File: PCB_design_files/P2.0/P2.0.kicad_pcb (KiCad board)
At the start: 4 copper layers, 18.5 x 18 mm, 58 parts, among them J1 EEG_IN, J2 20021121-00008C4LF, U1 INA819IDRGR, U2 TLV9102, U3 TPS61094, U4 TPS60400, U5 NRF52832-QFAA-R, Y1 32MHz

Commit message: Updated schematic
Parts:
- BT1, J1: moved to F.Cu
- C19, C20: footprint Capacitor_SMD:C_0402_1005Metric -> Capacitor_SMD:C_0603_1608Metric
- R20: moved to B.Cu
- moved C8 56.7 mm to (32.3, 77.2)
- moved L1 52.6 mm to (29.3, 67.6), turned to 180 degrees
- moved R19 52.0 mm to (32.5, 72.9), turned to 180 degrees
- moved U3 46.6 mm to (41.4, 71.5)
- moved C9 45.7 mm to (44.4, 69.7), turned to 90 degrees
- moved C10 44.7 mm to (46.6, 70.8)
- moved C11 41.7 mm to (46.4, 73.2)
- moved R17 39.9 mm to (113.0, 48.9), turned to 180 degrees
- moved U4 39.8 mm to (50.5, 71.1), turned to -90 degrees
- moved J2 39.7 mm to (77.7, 83.7)
- moved R16 38.2 mm to (113.0, 47.9), turned to 0 degrees
- moved C7 33.4 mm to (113.0, 46.9)
- moved R14 31.5 mm to (113.0, 45.9), turned to 0 degrees
- moved R12 30.0 mm to (92.0, 24.3), turned to 180 degrees
- moved R13 27.4 mm to (92.0, 26.3)
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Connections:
- U1 pad 9: (no net) -> -3V3
- U3 pad 13: (no net) -> GND
- U5 pad 49: unconnected-(U5-EPAD-Pad49) -> GND
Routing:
- net GND: track 39.9 -> 20.6 mm, vias 31 -> 13
- net Net-(BT1-+): track 16.2 -> 0.00 mm
- net +3V3: track 21.0 -> 4.83 mm, vias 7 -> 2
- net STAGE_3_OUT: track 7.70 -> 0.00 mm, vias 1 -> 0
- net /EEG+: track 6.87 -> 0.00 mm
- net /EEG-: track 6.62 -> 0.00 mm
- net Net-(U4-CFLY-): track 4.37 -> 0.00 mm
- net -3V3: track 5.62 -> 1.71 mm, vias 1 -> 0
- net Net-(U2-IN1+): track 3.07 -> 0.00 mm
- net Net-(U5-P0.02/AIN0): track 2.35 -> 0.00 mm
- net Net-(R3-Pad2): track 1.94 -> 0.00 mm
- net Net-(R3-Pad1): track 1.94 -> 0.00 mm
- net Net-(U4-CFLY+): track 1.71 -> 0.00 mm
- net Net-(C7-Pad1): track 1.50 -> 0.00 mm
- net Net-(U1-OUT): track 1.44 -> 0.00 mm
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- removed copper zone on B.Cu, net +3V3
- removed copper zone on B.Cu, net GND
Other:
- board size 18.5 x 18 mm -> 19 x 19 mm

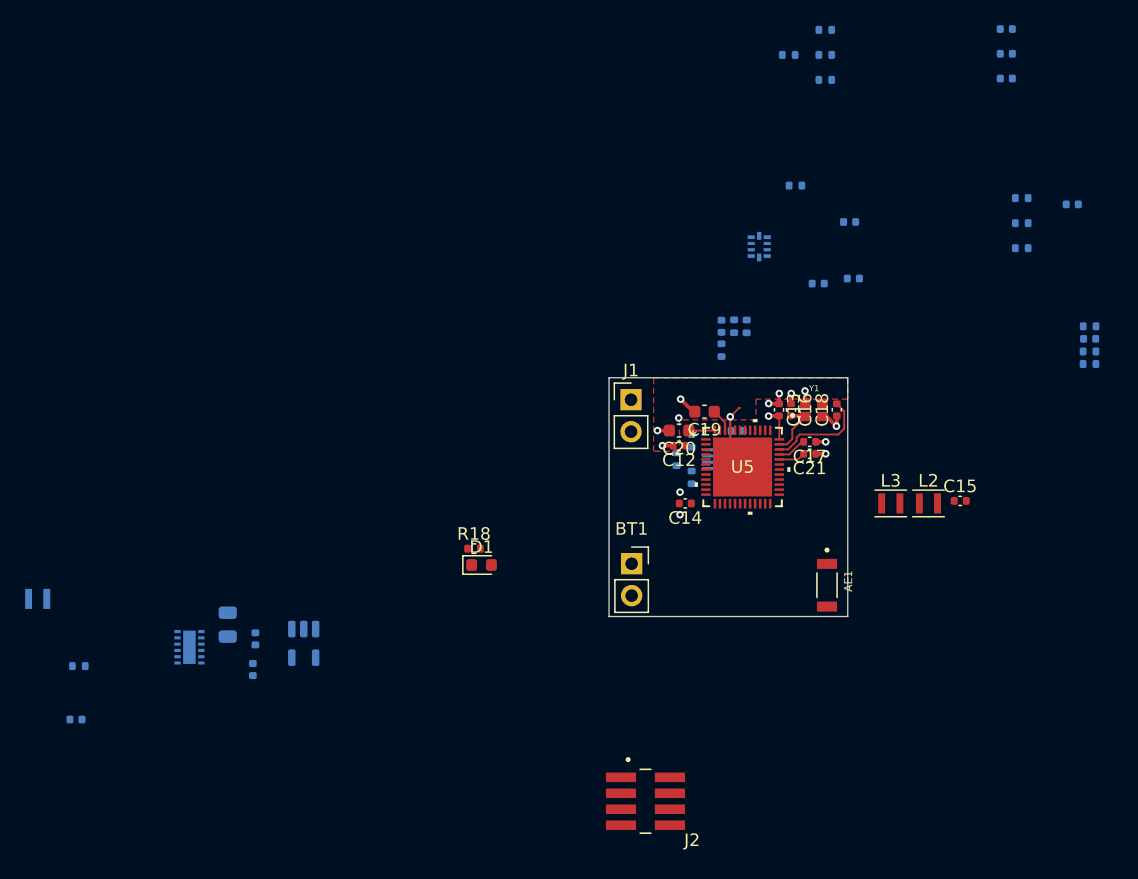
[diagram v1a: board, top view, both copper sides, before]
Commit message: made some schematic updates
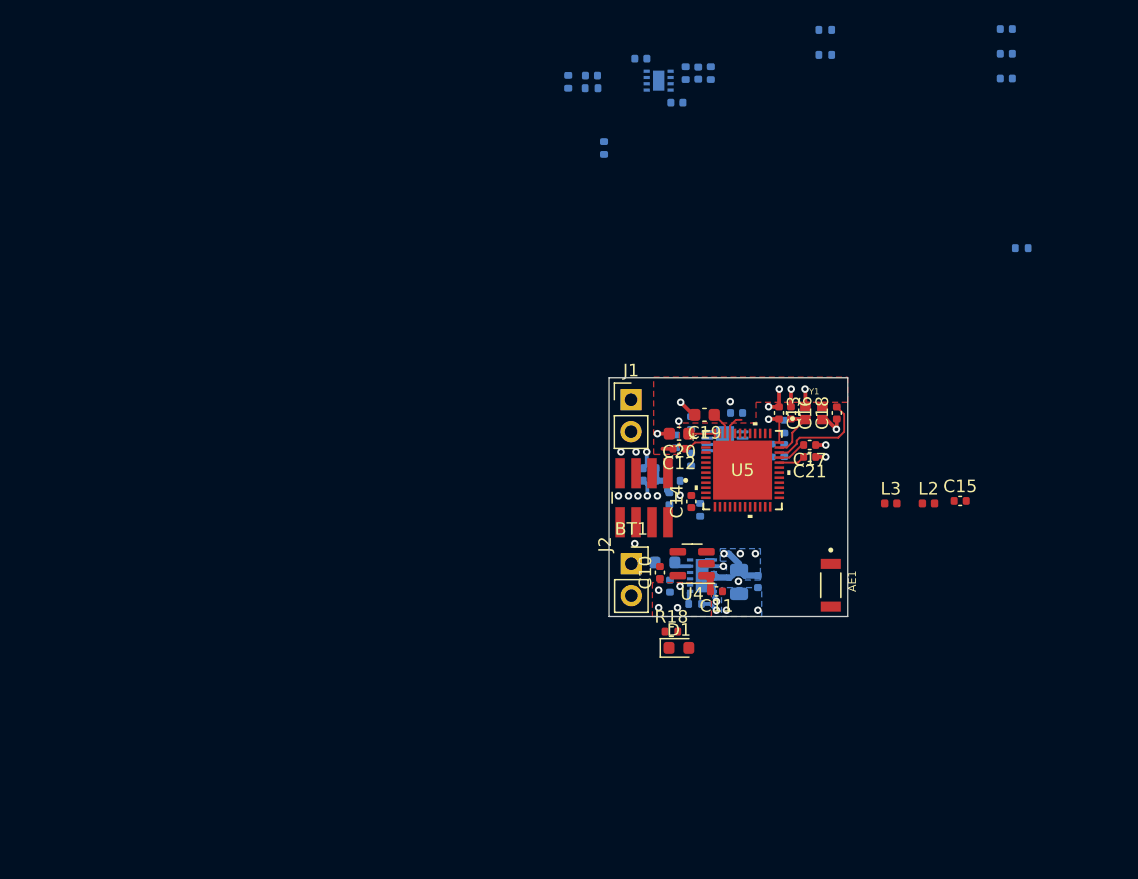
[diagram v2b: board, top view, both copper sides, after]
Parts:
- added C26: 0.1uF, Capacitor_SMD:C_0402_1005Metric, B.Cu at (86.6, 66.2)
- C10, C11, U4: moved to F.Cu
- C12, C13, C14: value 100nF -> 0.1uF
- C22, C23: value .1uF -> 0.1uF
- C24, C25: value .1uF -> 1uF
- L1: footprint Inductor_SMD:L_Murata_DFE201610P -> Inductor_SMD:L_0603_1608Metric
- L2, L3: footprint Inductor_SMD:L_Murata_DFE201610P -> Inductor_SMD:L_0402_1005Metric
- R19: value 1.1k -> 4.75k
- U2: value TLV9102 -> TLV9102IDSGR; footprint Package_DFN_QFN:Texas_R-PUQFN-N10 -> Package_SON:WSON-8-1EP_2x2mm_P0.5mm_EP0.9x1.6mm
- moved L1 50.0 mm to (79.2, 64.7), turned to 0 degrees
- moved R19 49.3 mm to (81.6, 68.0), turned to 0 degrees
- moved C8 48.5 mm to (79.6, 66.6), turned to 90 degrees
- moved U3 41.2 mm to (82.2, 65.8)
- moved C9 40.8 mm to (85.1, 66.2)
- moved C11 37.4 mm to (83.3, 67.0), turned to 180 degrees
- moved R16 36.5 mm to (78.0, 58.2), turned to 180 degrees
- moved R17 36.0 mm to (78.0, 57.2), turned to 0 degrees
- moved C7 35.8 mm to (79.5, 59.6), turned to 90 degrees
- moved R8 35.3 mm to (73.4, 26.9), turned to 0 degrees
- moved R20 35.1 mm to (79.9, 58.2), turned to 0 degrees
- moved R14 34.3 mm to (82.0, 60.5), turned to 90 degrees
- moved R9 33.8 mm to (74.3, 31.7), turned to -90 degrees
- moved C10 32.6 mm to (78.8, 65.5)
- moved U4 31.6 mm to (81.4, 64.8), turned to 180 degrees
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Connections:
- C2 pad 1: Net-(U2-IN1+) -> Net-(U2-OUT1)
- C24 pad 1: +3V3 -> GND
- C24 pad 2: GND -> -3V3
- C25 pad 2: -3V3 -> +3V3
- J2 pad 4: GND -> -3V3
- J2 pad 5: SWO -> NRST
- J2 pad 6: NRST -> SWO
- J2 pad 7: SWDIO -> SWDCLK
- J2 pad 8: SWDCLK -> SWDIO
- R6 pad 1: Net-(U2-IN1+) -> Net-(U2-OUT1)
- U1 pad 9: -3V3 -> (no net)
- U2 pad 1: -3V3 -> Net-(U2-OUT1)
- U2 pad 2: unconnected-(U2-SHDN1-Pad2) -> Net-(U2-IN1-)
- U2 pad 3: unconnected-(U2-SHDN2-Pad3) -> Net-(U2-IN1+)
- U2 pad 4: Net-(U2-IN2+) -> -3V3
- U2 pad 5: Net-(U2-IN2-) -> Net-(U2-IN2+)
- U2 pad 6: Net-(U2-OUT2) -> Net-(U2-IN2-)
- U2 pad 7: +3V3 -> Net-(U2-OUT2)
- U2 pad 8: Net-(U2-IN1+) -> +3V3
- U2 pad 9: Net-(U2-IN1-) -> (no net)
- U3 pad 13: GND -> (no net)
- U5 pad 49: GND -> unconnected-(U5-EPAD-Pad49)
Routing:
- net +3V3: track 4.83 -> 16.8 mm, vias 2 -> 6
- net GND: track 20.6 -> 26.1 mm, vias 13 -> 21
- net STAGE_3_OUT: track 0.00 -> 2.90 mm
- net Net-(U5-DEC1): track 0.00 -> 1.86 mm
- net Net-(U3-SW): track 0.00 -> 1.34 mm
- net Net-(U3-OSEL): track 0.00 -> 1.05 mm
- net -3V3: track 1.71 -> 1.38 mm, vias 0 -> 4
- net SWO: vias 0 -> 1
- net SWDIO: vias 0 -> 1
- net SWDCLK: vias 0 -> 1
- net NRST: vias 0 -> 1
- added copper zone on B.Cu, net +3V3
- added copper zone on F.Cu, net -3V3
- added copper zone on B.Cu, net GND

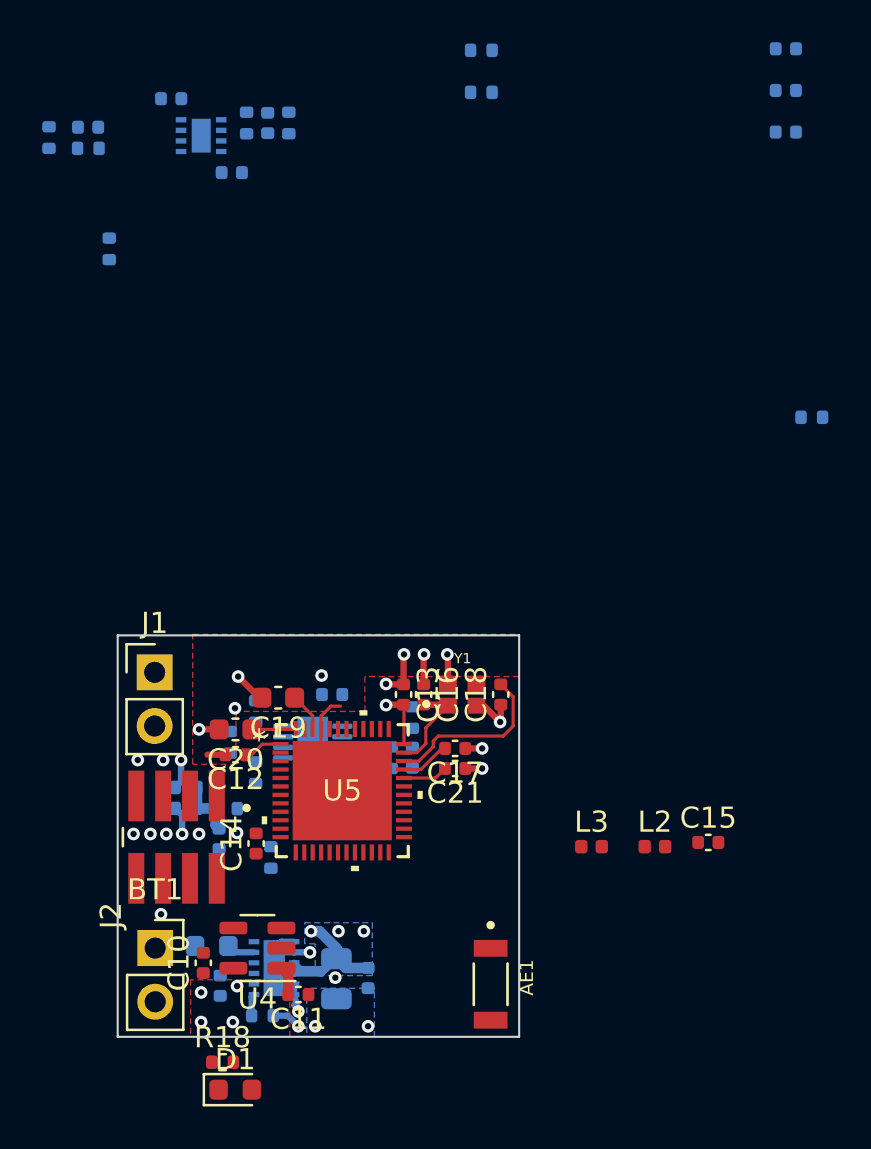
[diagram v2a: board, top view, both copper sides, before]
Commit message: Schematic updates
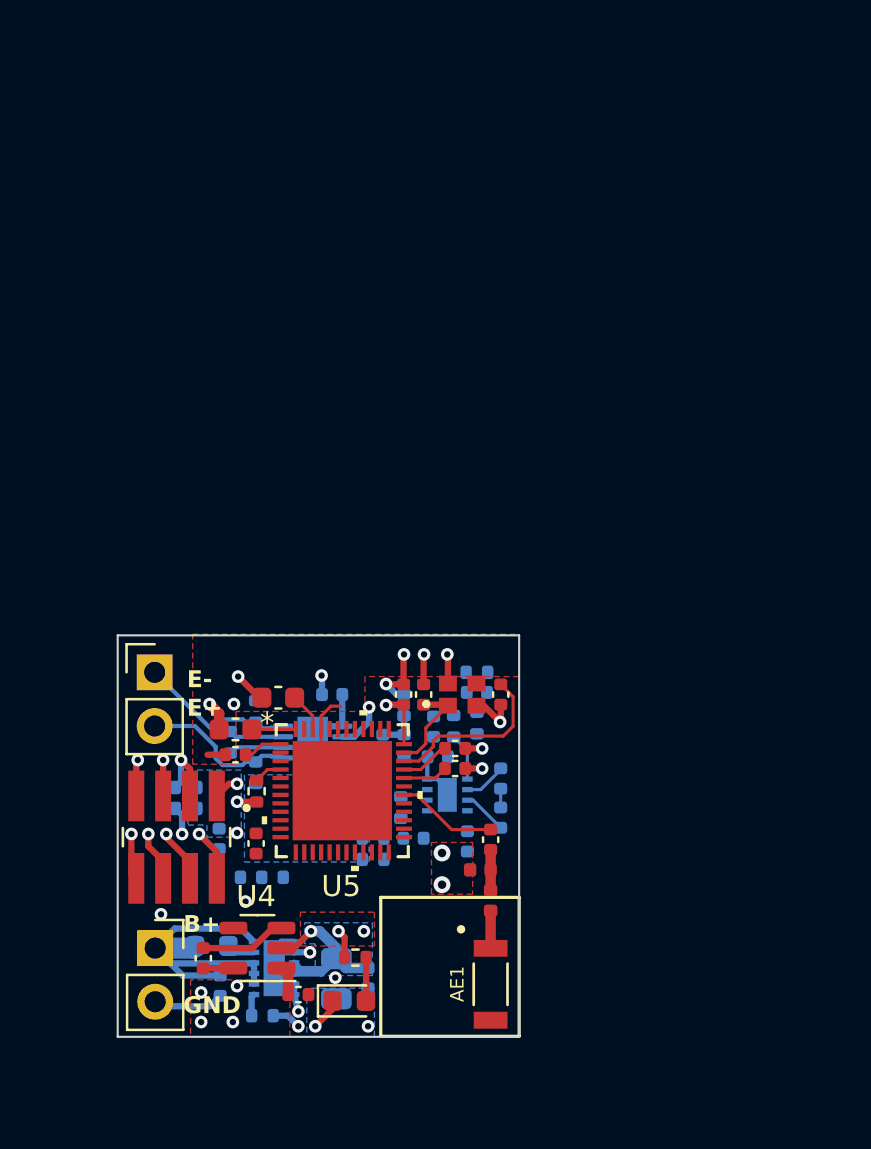
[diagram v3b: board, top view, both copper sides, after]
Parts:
- R20: moved to F.Cu
- moved C3 38.1 mm to (92.9, 58.6), turned to 90 degrees
- moved C25 37.8 mm to (91.3, 59.8), turned to 90 degrees
- moved R13 36.6 mm to (82.1, 61.5), turned to 0 degrees
- moved C4 36.2 mm to (89.7, 54.3), turned to -90 degrees
- moved C2 34.5 mm to (88.8, 59.6), turned to 180 degrees
- moved C6 33.4 mm to (92.9, 56.8), turned to -90 degrees
- moved U2 33.3 mm to (90.3, 57.5), turned to 0 degrees
- moved R6 33.2 mm to (88.2, 58.1), turned to 90 degrees
- moved R7 32.1 mm to (86.8, 57.6), turned to 180 degrees
- moved C5 32.0 mm to (91.8, 52.7), turned to 0 degrees
- moved R11 32.0 mm to (90.7, 54.3), turned to -90 degrees
- moved R8 30.9 mm to (91.8, 51.8), turned to 180 degrees
- moved R9 30.6 mm to (86.8, 59.6), turned to 180 degrees
- moved R12 29.9 mm to (91.8, 54.1), turned to -90 degrees
- moved R10 29.5 mm to (86.8, 60.6)
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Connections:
- R18 pad 1: Net-(BT1-+) -> +3V3
- U1 pad 9: (no net) -> -3V3
- U2 pad 9: (no net) -> -3V3
- U5 pad 49: unconnected-(U5-EPAD-Pad49) -> GND
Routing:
- net Net-(BT1-+): track 0.00 -> 16.8 mm
- net GND: track 26.1 -> 37.0 mm, vias 21 -> 25
- net /EEG-: track 0.00 -> 8.10 mm
- net -3V3: track 1.38 -> 8.80 mm
- net /EEG+: track 0.00 -> 7.39 mm
- net Net-(U5-ANT): track 0.00 -> 4.78 mm
- net +3V3: track 16.8 -> 21.6 mm
- net Net-(U4-CFLY-): track 0.00 -> 4.09 mm
- net Net-(R3-Pad1): track 0.00 -> 2.61 mm
- net Net-(R3-Pad2): track 0.00 -> 2.60 mm
- net SWDCLK: track 0.00 -> 2.56 mm
- net SWDIO: track 0.00 -> 2.45 mm
- net SWO: track 0.00 -> 2.39 mm
- net Net-(U2-IN2+): track 0.00 -> 2.26 mm
- net NRST: track 0.00 -> 2.20 mm
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- added copper zone on F.Cu, net +3V3
- added copper zone on B.Cu, net STAGE_3_OUT
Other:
- board text added: "B+"
- board text added: "E+"
- board text added: "E-"
- board text added: "GND"

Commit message: Updated schematic
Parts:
- removed C21: ~, Capacitor_SMD:C_0402_1005Metric
- J2: value 20021121-00008C4LF -> Conn_02x03_Counter_Clockwise; footprint 20021121_00008C4LF:AMPHENOL_20021121-00008C4LF -> 20021121_00006C4LF:AMPHENOL_20021121-00006C4LF
- R13: moved to F.Cu
- moved R13 11.4 mm to (92.7, 57.3), turned to -90 degrees
- moved C17 1.27 mm to (90.0, 56.4)
- moved R14 1.05 mm to (79.0, 61.5), turned to 0 degrees
- moved L2 0.92 mm to (93.3, 62.7)
- moved C15 0.91 mm to (93.3, 59.8)
- moved L3 0.91 mm to (92.8, 61.2)
- moved AE1 0.91 mm to (93.3, 66.7)
- moved C2 0.71 mm to (88.7, 60.3)
- moved J2 0.56 mm to (77.0, 59.5), turned to 0 degrees
- moved R10 0.30 mm to (86.8, 60.3)
- moved R9 0.30 mm to (86.8, 59.3)
- moved C4 0.15 mm to (89.8, 54.3)
- moved R11 0.15 mm to (90.8, 54.3)
- moved C14 0.07 mm to (81.3, 59.8)
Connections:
- J2 pad 1: STAGE_3_OUT -> -3V3
- J2 pad 3: GND -> STAGE_3_OUT
- J2 pad 4: -3V3 -> SWDIO
- J2 pad 5: NRST -> SWDCLK
- J2 pad 6: SWO -> GND
- U3 pad 13: (no net) -> GND
- U5 pad 21: SWO -> unconnected-(U5-P0.18/TRACEDATA[0]/SWO-Pad21)
- U5 pad 24: NRST -> unconnected-(U5-P0.21/Nreset-Pad24)
- U5 pad 32: Net-(U5-DEC2) -> unconnected-(U5-DEC2-Pad32)
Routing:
- net -3V3: track 8.80 -> 50.8 mm, vias 4 -> 5
- net Net-(C3-Pad2): track 0.89 -> 42.3 mm, vias 0 -> 1
- net Net-(C5-Pad1): track 0.00 -> 25.8 mm, vias 0 -> 2
- net SWDCLK: track 2.56 -> 14.9 mm, vias 1 -> 0
- net +3V3: track 21.6 -> 33.7 mm, vias 6 -> 9
- net GND: track 37.0 -> 48.8 mm, vias 25 -> 31
- net SWDIO: track 2.45 -> 13.8 mm, vias 1 -> 0
- net Net-(U2-IN2-): track 2.03 -> 5.61 mm, vias 0 -> 1
- net Net-(U2-OUT1): track 0.00 -> 3.51 mm
- net SWO: track 2.39 -> 0.00 mm, vias 1 -> 0
- net Net-(U2-IN1+): track 0.00 -> 2.33 mm
- net Net-(U2-IN1-): track 0.00 -> 2.21 mm
- net NRST: track 2.20 -> 0.00 mm, vias 1 -> 0
- net Net-(U5-DEC2): track 2.13 -> 0.00 mm
- net Net-(C2-Pad2): track 0.00 -> 1.87 mm
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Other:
- board size 19 x 19 mm -> 19.8 x 19.5 mm
- board text added: "ANT"
- board text added: "JY-68 P2.0"
